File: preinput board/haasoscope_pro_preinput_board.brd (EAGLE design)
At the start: 94.2 x 77.8 mm, 44 parts, among them J1 test1, J2 8pin, J4 8pin, K1 AQY21SOP, K2 G6K-2F-RF-DC3, K3 G6K-2F-RF-DC3, K4 G6K-2F-RF-DC3, Q1 S8050, Q2 S8050, Q3 S8050

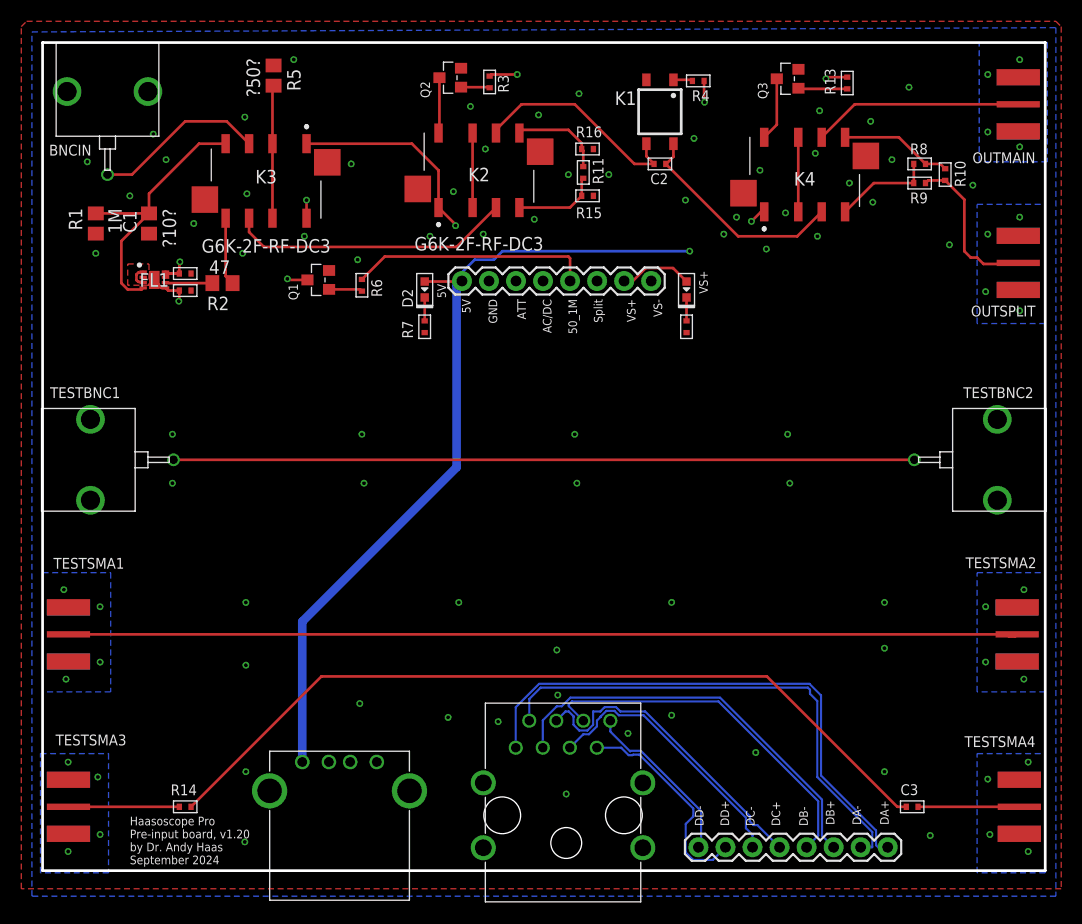
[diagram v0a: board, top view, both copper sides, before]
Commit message: add -T relay, and new ACDC SSR
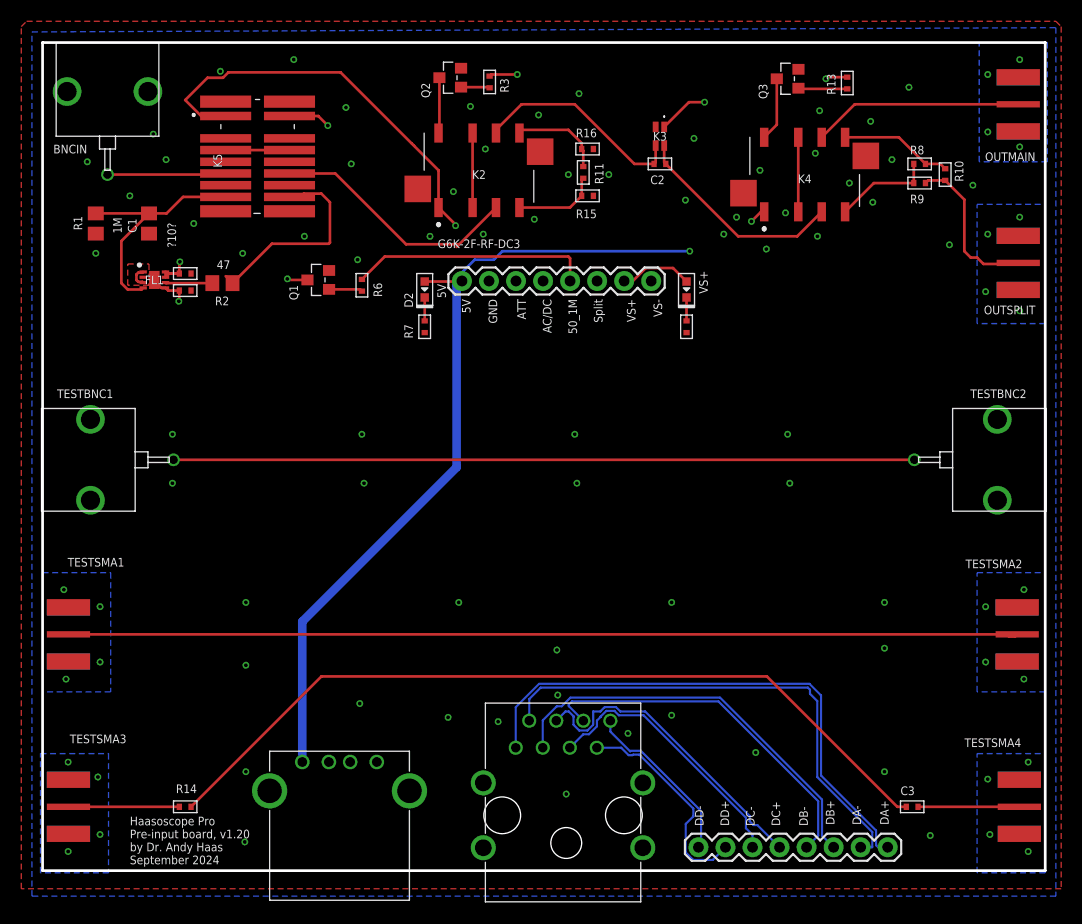
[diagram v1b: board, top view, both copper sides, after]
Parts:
- removed K1: AQY21SOP, relay:SOP04
- removed R4: 1k, MF_Passives:R0402
- removed R5: ?50?, resistor:R0805
- added K5: G6K-2F-RF-T-TR03_DC5, G6K-2F-RF-T-TR03_DC5:G6K2FRFTTR03DC5
- K3: value G6K-2F-RF-DC3 -> TLP3440_TP,F; device G6K-2F-RF-DC3:G6K2FRFDC3 -> TLP3440_TP_F:TLP3440TPF
- moved K3 37.2 mm to (48.8, 41.2)
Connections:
- removed net N$11: K1.1, R4.P$1
- net 1MPATH: now also K5.4; no longer K3.4
- net 1MPATH50: now also K5.5; no longer K3.5
- net 50PATH: now also K5.2, K5.7; no longer K3.2, K3.7, R5.2
- net 5V: now also K5.1; no longer K3.1
- net ACDC_CONTROL: now also K3.1; no longer R4.P$2
- net COIL1-: now also K5.8; no longer K3.8
- net GND: now also K3.2, K5.MP1, K5.MP10, K5.MP2, K5.MP3, K5.MP4, K5.MP5, K5.MP6, K5.MP7, K5.MP8, K5.MP9; no longer K1.2, K3.MP1, K3.MP2, R5.1
- net INPATH: now also K5.3; no longer K3.3
- net OUTPATH: now also K5.6; no longer K3.6
- net OUTPATHACDC: now also K3.4; no longer K1.4
- net OUTPATHFILT: now also K3.3; no longer K1.3
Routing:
- net 5V: track 111.3 -> 131.0 mm
- net 1MPATH50: track 6.37 -> 19.7 mm
- net COIL1-: track 11.8 -> 21.9 mm
- net 50PATH: track 12.5 -> 6.60 mm
- net INPATH: track 16.2 -> 11.3 mm
- net 1MPATH: track 26.0 -> 22.8 mm
- net ACDC_CONTROL: track 25.1 -> 27.9 mm
- net OUTPATH: track 26.6 -> 24.5 mm
- net N$11: track 1.82 -> 0.00 mm

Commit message: use new T relays, re-layout
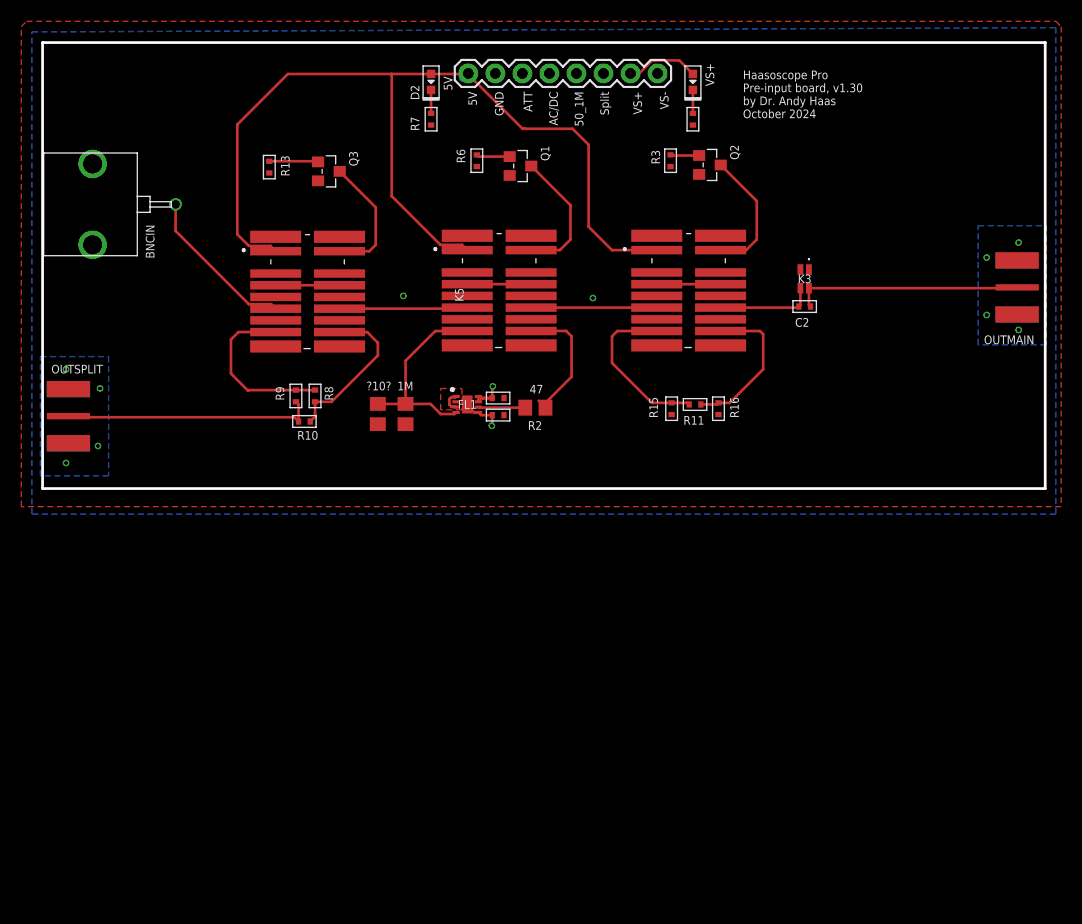
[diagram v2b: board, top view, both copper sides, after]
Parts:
- removed C3: 1uF, MF_Passives:C0402
- removed J1: test1, FlashPCB_Connectors:USB-2.0-A-THT-RA-TE_AMP-292303-1
- removed J2: 8pin, SparkFun-Connectors:1X08
- removed K4: G6K-2F-RF-DC3, G6K-2F-RF-DC3:G6K2FRFDC3
- removed R14: 0, MF_Passives:R0402
- removed TESTBNC1, TESTBNC2: MOLEX_BNC_73100-0105, connector:MOLEX-BNC-73100-0105
- removed TESTSMA1, TESTSMA2, TESTSMA3, TESTSMA4: out50, adafruit:SMA_EDGELAUNCH
- removed U$1: RJ45-CONNECTOR-SHIELDED, FlashPCB_Connectors:RJ45_THT_RA_AMPH-FRJAE448
- added K1: G6K-2F-RF-T-TR03_DC5, G6K-2F-RF-T-TR03_DC5:G6K2FRFTTR03DC5
- K2: value G6K-2F-RF-DC3 -> G6K-2F-RF-T-TR03_DC5; device G6K-2F-RF-DC3:G6K2FRFDC3 -> G6K-2F-RF-T-TR03_DC5:G6K2FRFTTR03DC5
- moved OUTSPLIT 94.4 mm to (-8.80, 14.9), turned to 0 degrees
- moved R10 64.5 mm to (15.4, 14.4), turned to 180 degrees
- moved R9 61.9 mm to (14.6, 16.8), turned to 270 degrees
- moved R8 60.8 mm to (16.4, 16.8), turned to 270 degrees
- moved R13 54.9 mm to (12.1, 38.3), turned to 270 degrees
- moved Q3 44.0 mm to (17.7, 37.9), turned to 270 degrees
- moved R1 34.2 mm to (24.9, 15.1)
- moved C11 31.6 mm to (33.6, 16.6)
- moved C12 31.6 mm to (33.6, 15.0)
- moved R2 31.6 mm to (37.1, 15.7)
- moved FL1 31.6 mm to (30.7, 16.0)
- moved C1 28.0 mm to (22.3, 15.1)
- moved R16 27.3 mm to (54.3, 15.6), turned to 270 degrees
- moved K5 26.0 mm to (33.7, 25.1)
- moved Q2 25.7 mm to (53.5, 38.5), turned to 270 degrees
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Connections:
- removed net DA_N: J2.2, U$1.P$2
- removed net DA_P: J2.1, U$1.P$1
- removed net DB_N: J2.4, U$1.P$6
- removed net DB_P: J2.3, U$1.P$3
- removed net DC_N: J2.6, U$1.P$5
- removed net DC_P: J2.5, U$1.P$4
- removed net DD_N: J2.8, U$1.P$8
- removed net DD_P: J2.7, U$1.P$7
- removed net N$10: R14.P$2, TESTSMA3.P
- removed net N$12: C3.P$1, R14.P$1
- removed net N$13: C3.P$2, TESTSMA4.P
- removed net N$8: TESTBNC1.SIGNAL, TESTBNC2.SIGNAL
- removed net N$9: TESTSMA1.P, TESTSMA2.P
- removed net OUTPATHACDC: C2.P$2, K3.4, K4.3
- new net OUTSPLITTER: K1.6, K5.3
- net 5V: now also K1.1; no longer J1.P$1, K4.1
- net COIL3-: now also K1.8; no longer K4.8
- net GND: now also K1.MP1, K1.MP10, K1.MP2, K1.MP3, K1.MP4, K1.MP5, K1.MP6, K1.MP7, K1.MP8, K1.MP9, K2.MP10, K2.MP3, K2.MP4, K2.MP5, K2.MP6, K2.MP7, K2.MP8, K2.MP9; no longer J1.P$4, K4.MP1, K4.MP2, TESTBNC1.GND1, TESTBNC1.GND2, TESTBNC2.GND1, TESTBNC2.GND2, TESTSMA1.GND@1, TESTSMA1.GND@2, TESTSMA1.GND@3, TESTSMA1.GND@4, TESTSMA2.GND@1, TESTSMA2.GND@2, TESTSMA2.GND@3, TESTSMA2.GND@4, TESTSMA3.GND@1, TESTSMA3.GND@2, TESTSMA3.GND@3, TESTSMA3.GND@4, TESTSMA4.GND@1, TESTSMA4.GND@2, TESTSMA4.GND@3, TESTSMA4.GND@4, U$1.S$1, U$1.S$2, U$1.S$3, U$1.S$4
- net INPATH: now also K1.3; no longer K5.3
- net NOSPLIT: now also K1.2, K1.7; no longer K4.2, K4.7
- net OUTMAIN: now also C2.P$2, K3.4; no longer K4.6
- net SPLIT: now also K1.4; no longer K4.4
- net SPLITOUT: now also K1.5; no longer K4.5
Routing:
- net N$9: track 89.3 -> 0.00 mm
- net N$12: track 77.3 -> 0.00 mm
- net N$8: track 69.6 -> 0.00 mm
- net DA_P: track 51.2 -> 0.00 mm
- net DA_N: track 47.2 -> 0.00 mm
- net 5V: track 131.0 -> 91.9 mm, vias 3 -> 0
- net DB_P: track 38.6 -> 0.00 mm
- net DB_N: track 34.3 -> 0.00 mm
- net SPLIT_CONTROL: track 32.0 -> 0.90 mm, vias 1 -> 0
- net DC_P: track 29.9 -> 0.00 mm
- net ACDC_CONTROL: track 27.9 -> 1.62 mm, vias 1 -> 0
- net DC_N: track 25.5 -> 0.00 mm
- net 50_1M_CONTROL: track 22.7 -> 0.00 mm
- net ATT_CONTROL: track 22.1 -> 0.38 mm, vias 1 -> 0
- net DD_P: track 20.4 -> 0.00 mm
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- removed copper zone on layer 15, net GND
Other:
- board size 94.2 x 77.8 mm -> 94.2 x 41.9 mm
- board text added: "Haasoscope Pro Pre-input board, v1.30 by Dr. Andy Haas October 2024"
- board text removed: "DA+"
- board text removed: "DA-"
- board text removed: "DB+"
- board text removed: "DB-"
- board text removed: "DC+"
- board text removed: "DC-"
- board text removed: "DD+"
- board text removed: "DD-"
- board text removed: "Haasoscope Pro Pre-input board, v1.20 by Dr. Andy Haas September 2024"

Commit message: finish routing
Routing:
- net SPLIT_CONTROL: track 0.90 -> 40.0 mm, vias 0 -> 1
- net ACDC_CONTROL: track 1.62 -> 35.4 mm
- net ATT_CONTROL: track 0.38 -> 17.9 mm
- net 50_1M_CONTROL: track 0.00 -> 14.7 mm, vias 0 -> 1
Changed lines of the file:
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@@
 <layer number="27" name="tValues" color="7" fill="1" visible="yes" active="yes"/>
 <layer number="28" name="bValues" color="7" fill="1" visible="yes" active="yes"/>
-<layer number="29" name="tStop" color="7" fill="3" visible="yes" active="yes"/>
-<layer number="30" name="bStop" color="7" fill="6" visible="yes" active="yes"/>
-<layer number="31" name="tCream" color="7" fill="4" visible="yes" active="yes"/>
-<layer number="32" name="bCream" color="7" fill="5" visible="yes" active="yes"/>
-<layer number="33" name="tFinish" color="6" fill="3" visible="yes" active="yes"/>
-<layer number="34" name="bFinish" color="6" fill="6" visible="yes" active="yes"/>
-<layer number="35" name="tGlue" color="7" fill="4" visible="yes" active="yes"/>
-<layer number="36" name="bGlue" color="7" fill="5" visible="yes" active="yes"/>
-<layer number="37" name="tTest" color="7" fill="1" visible="yes" active="yes"/>
-<layer number="38" name="bTest" color="7" fill="1" visible="yes" active="yes"/>
+<layer number="29" name="tStop" color="7" fill="3" visible="no" active="yes"/>
+<layer number="30" name="bStop" color="7" fill="6" visible="no" active="yes"/>
+<layer number="31" name="tCream" color="7" fill="4" visible="no" active="yes"/>
+<layer number="32" name="bCream" color="7" fill="5" visible="no" active="yes"/>
+<layer number="33" name="tFinish" color="6" fill="3" visible="no" active="yes"/>
+<layer number="34" name="bFinish" color="6" fill="6" visible="no" active="yes"/>
+<layer number="35" name="tGlue" color="7" fill="4" visible="no" active="yes"/>
+<layer number="36" name="bGlue" color="7" fill="5" visible="no" active="yes"/>
+<layer number="37" name="tTest" color="7" fill="1" visible="no" active="yes"/>
+<layer number="38" name="bTest" color="7" fill="1" visible="no" active="yes"/>
 <layer number="39" name="tKeepout" color="4" fill="11" visible="yes" active="yes"/>
 <layer number="40" name="bKeepout" color="1" fill="11" visible="yes" active="yes"/>
 <layer number="41" name="tRestrict" color="4" fill="10" visible="yes" active="yes"/>
 <layer number="42" name="bRestrict" color="1" fill="10" visible="yes" active="yes"/>
-<layer number="43" name="vRestrict" color="2" fill="10" visible="yes" active="yes"/>
-<layer number="44" name="Drills" color="7" fill="1" visible="yes" active="yes"/>
-<layer number="45" name="Holes" color="7" fill="1" visible="yes" active="yes"/>
-<layer number="46" name="Milling" color="3" fill="1" visible="yes" active="yes"/>
-<layer number="47" name="Measures" color="7" fill="1" visible="yes" active="yes"/>
-<layer number="48" name="Document" color="7" fill="1" visible="yes" active="yes"/>
-<layer number="49" name="Reference" color="7" fill="1" visible="yes" active="yes"/>
+<layer number="43" name="vRestrict" color="2" fill="10" visible="no" active="yes"/>
+<layer number="44" name="Drills" color="7" fill="1" visible="no" active="yes"/>
+<layer number="45" name="Holes" color="7" fill="1" visible="no" active="yes"/>
+<layer number="46" name="Milling" color="3" fill="1" visible="no" active="yes"/>
+<layer number="47" name="Measures" color="7" fill="1" visible="no" active="yes"/>
+<layer number="48" name="Document" color="7" fill="1" visible="no" active="yes"/>
+<layer number="49" name="Reference" color="7" fill="1" visible="no" active="yes"/>
 <layer number="50" name="dxf" color="7" fill="1" visible="no" active="no"/>
 <layer number="51" name="tDocu" color="7" fill="1" visible="yes" active="yes"/>
@@
 <layer number="134" name="silk_top" color="7" fill="1" visible="no" active="no"/>
 <layer number="135" name="silk_bottom" color="7" fill="1" visible="no" active="no"/>
-<layer number="136" name="silktop" color="7" fill="1" visible="yes" active="yes"/>
-<layer number="137" name="silkbottom" color="7" fill="1" visible="yes" active="yes"/>
+<layer number="136" name="silktop" color="7" fill="1" visible="no" active="yes"/>
+<layer number="137" name="silkbottom" color="7" fill="1" visible="no" active="yes"/>
 <layer number="144" name="DrillLegend" color="7" fill="1" visible="no" active="no"/>
-<layer number="145" name="DrillLegend_01-16" color="7" fill="1" visible="yes" active="yes"/>
-<layer number="146" name="DrillLegend_01-20" color="7" fill="1" visible="yes" active="yes"/>
+<layer number="145" name="DrillLegend_01-16" color="7" fill="1" visible="no" active="yes"/>
+<layer number="146" name="DrillLegend_01-20" color="7" fill="1" visible="no" active="yes"/>
 <layer number="150" name="Notes" color="7" fill="1" visible="no" active="no"/>
 <layer number="151" name="HeatSink" color="14" fill="1" visible="no" active="no"/>
@@
 <layer number="154" name="FabDoc2" color="2" fill="1" visible="no" active="no"/>
 <layer number="155" name="FabDoc3" color="7" fill="15" visible="no" active="no"/>
-<layer number="166" name="AntennaArea" color="7" fill="1" visible="yes" active="yes"/>
-<layer number="168" name="4mmHeightArea" color="7" fill="1" visible="yes" active="yes"/>
+<layer number="166" name="AntennaArea" color="7" fill="1" visible="no" active="yes"/>
+<layer number="168" name="4mmHeightArea" color="7" fill="1" visible="no" active="yes"/>
 <layer number="199" name="Contour" color="7" fill="1" visible="no" active="no"/>
 <layer number="200" name="200bmp" color="1" fill="10" visible="no" active="no"/>
@@
 <wire x1="38.42" y1="48.72" x2="38.42" y2="47.1" width="0.254" layer="15"/>
 <contactref element="K3" pad="1"/>
-<wire x1="38.42" y1="47.1" x2="62.8" y2="28.675" width="0" layer="19" extent="1-1"/>
+<wire x1="62.8" y1="28.675" x2="62.5544" y2="28.9206" width="0.254" layer="1"/>
+<wire x1="39.2357875" y1="47.1" x2="38.42" y2="47.1" width="0.254" layer="1"/>
+<wire x1="62.5544" y1="28.9206" x2="62.5544" y2="31.93623125" width="0.254" layer="1"/>
+<wire x1="62.5544" y1="31.93623125" x2="54.31423125" y2="40.1764" width="0.254" layer="1"/>
+<wire x1="54.31423125" y1="40.1764" x2="46.1593875" y2="40.1764" width="0.254" layer="1"/>
+<wire x1="46.1593875" y1="40.1764" x2="39.2357875" y2="47.1" width="0.254" layer="1"/>
 </signal>
 <signal name="50_1M_CONTROL">
 <contactref element="J4" pad="5"/>
 <contactref element="R6" pad="P$2"/>
-<wire x1="31.6" y1="38.35" x2="40.96" y2="47.1" width="0" layer="19" extent="1-1"/>
+<via x="32.9" y="41.6" extent="1-16" drill="0.35"/>
+<wire x1="31.0206" y1="39.08426875" x2="31.0206" y2="39.81573125" width="0.254" layer="1"/>
+<wire x1="31.0206" y1="39.81573125" x2="31.18426875" y2="39.9794" width="0.254" layer="1"/>
+<wire x1="31.18426875" y1="39.9794" x2="31.2794" y2="39.9794" width="0.254" layer="1"/>
+<wire x1="31.2794" y1="39.9794" x2="32.9" y2="41.6" width="0.254" layer="1"/>
+<wire x1="31.6" y1="38.35" x2="31.6" y2="38.50486875" width="0.254" layer="1"/>
+<wire x1="31.6" y1="38.50486875" x2="31.0206" y2="39.08426875" width="0.254" layer="1"/>
+<wire x1="32.9" y1="41.6" x2="37.1808" y2="45.8808" width="0.254" layer="16"/>
+<wire x1="40.1442125" y1="47.1" x2="40.96" y2="47.1" width="0.254" layer="16"/>
+<wire x1="37.1808" y1="45.8808" x2="38.9250125" y2="45.8808" width="0.254" layer="16"/>
+<wire x1="38.9250125" y1="45.8808" x2="40.1442125" y2="47.1" width="0.254" layer="16"/>
 </signal>
 <signal name="1MPATH">
@@
 <contactref element="J4" pad="3"/>
 <contactref element="R3" pad="P$2"/>
-<wire x1="49.8" y1="38.35" x2="49.65" y2="38.2" width="0.254" layer="1"/>
+<wire x1="49.65" y1="38.2" x2="49.8" y2="38.35" width="0.254" layer="1"/>
 <wire x1="36" y1="47.22" x2="35.88" y2="47.1" width="0.254" layer="15"/>
-<wire x1="36" y1="47.22" x2="49.65" y2="38.2" width="0" layer="19" extent="1-15"/>
+<wire x1="35.88" y1="47.1" x2="40.6736" y2="42.3064" width="0.254" layer="1"/>
+<wire x1="40.6736" y1="42.3064" x2="40.7683375" y2="42.3064" width="0.254" layer="1"/>
+<wire x1="44.7247375" y1="38.35" x2="49.8" y2="38.35" width="0.254" layer="1"/>
+<wire x1="40.7683375" y1="42.3064" x2="44.7247375" y2="38.35" width="0.254" layer="1"/>
 </signal>
 <signal name="COIL2-">
@@
 <contactref element="J4" pad="6"/>
 <wire x1="43.5" y1="48" x2="43.5" y2="47.1" width="0.254" layer="15"/>
-<wire x1="12.1" y1="37.75" x2="43.5" y2="47.1" width="0" layer="19" extent="1-1"/>
+<via x="19.2" y="43.9" extent="1-16" drill="0.35"/>
+<wire x1="11.5206" y1="38.48426875" x2="11.5206" y2="39.21573125" width="0.254" layer="1"/>
+<wire x1="11.5206" y1="39.21573125" x2="16.20486875" y2="43.9" width="0.254" layer="1"/>
+<wire x1="16.20486875" y1="43.9" x2="19.2" y2="43.9" width="0.254" layer="1"/>
+<wire x1="12.1" y1="37.75" x2="12.1" y2="37.90486875" width="0.254" layer="1"/>
+<wire x1="12.1" y1="37.90486875" x2="11.5206" y2="38.48426875" width="0.254" layer="1"/>
+<wire x1="19.2" y1="43.9" x2="42.9" y2="43.9" width="0.254" layer="15"/>
+<wire x1="42.9" y1="43.9" x2="43.2" y2="43.6" width="0.254" layer="15"/>
+<wire x1="43.2" y1="43.6" x2="43.5" y2="43.9" width="0.254" layer="15"/>
+<wire x1="43.5" y1="43.9" x2="43.5" y2="47.1" width="0.254" layer="15"/>
 </signal>
 <signal name="COIL3-">
